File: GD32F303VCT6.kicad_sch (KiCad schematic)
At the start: 32 parts, among them SW1 SKRPACE010, U6 GD32F303VCT6, Y1 TAXM8M4RDBCCT2T, Y2 XKXGI-SUA-32.768K

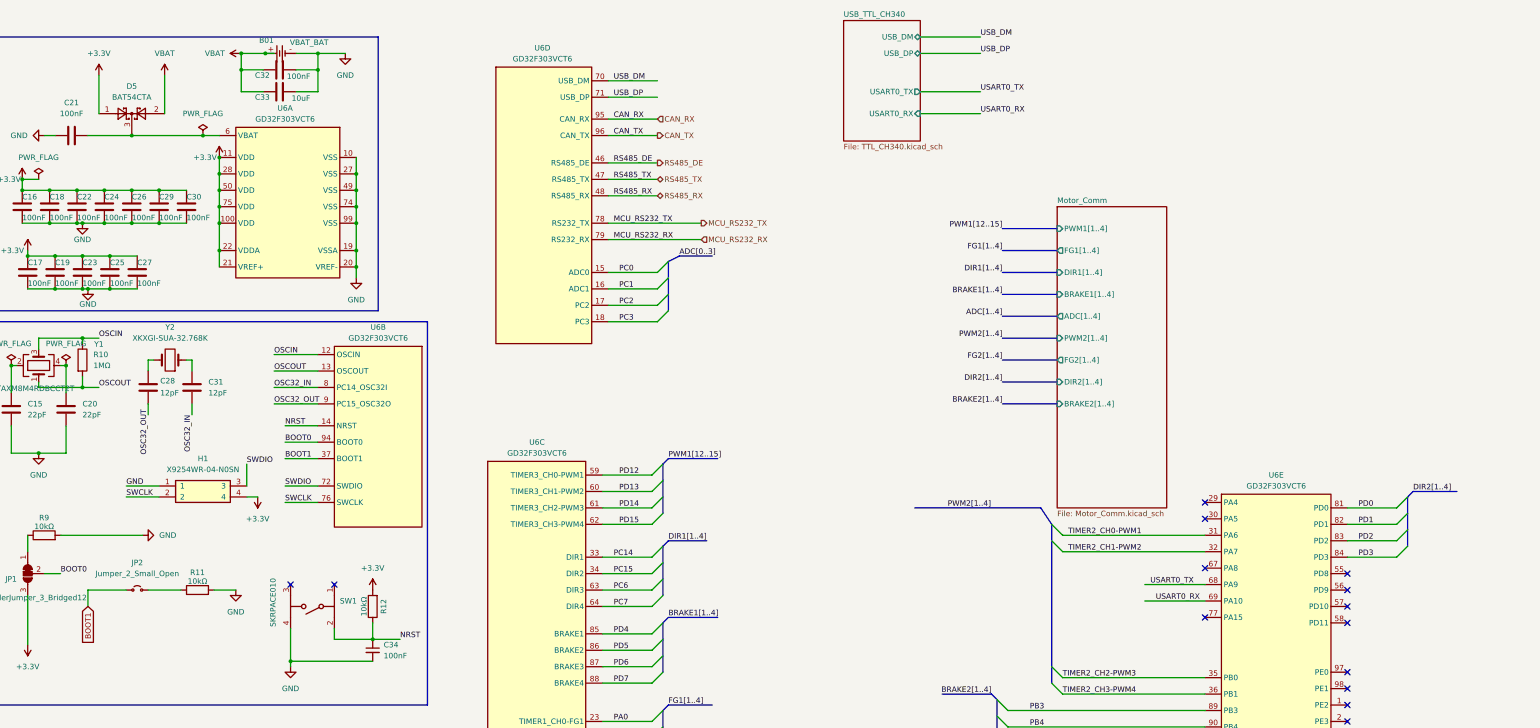
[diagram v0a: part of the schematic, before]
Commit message: 完成GD32F303控制板原理图与PCB设计
- 更新电源、CAN、RS232、RS485及电机通信子电路
- 切换并完善GD32F303VCT6核心原理图
- 新增PCB布局及所需符号、封装库文件
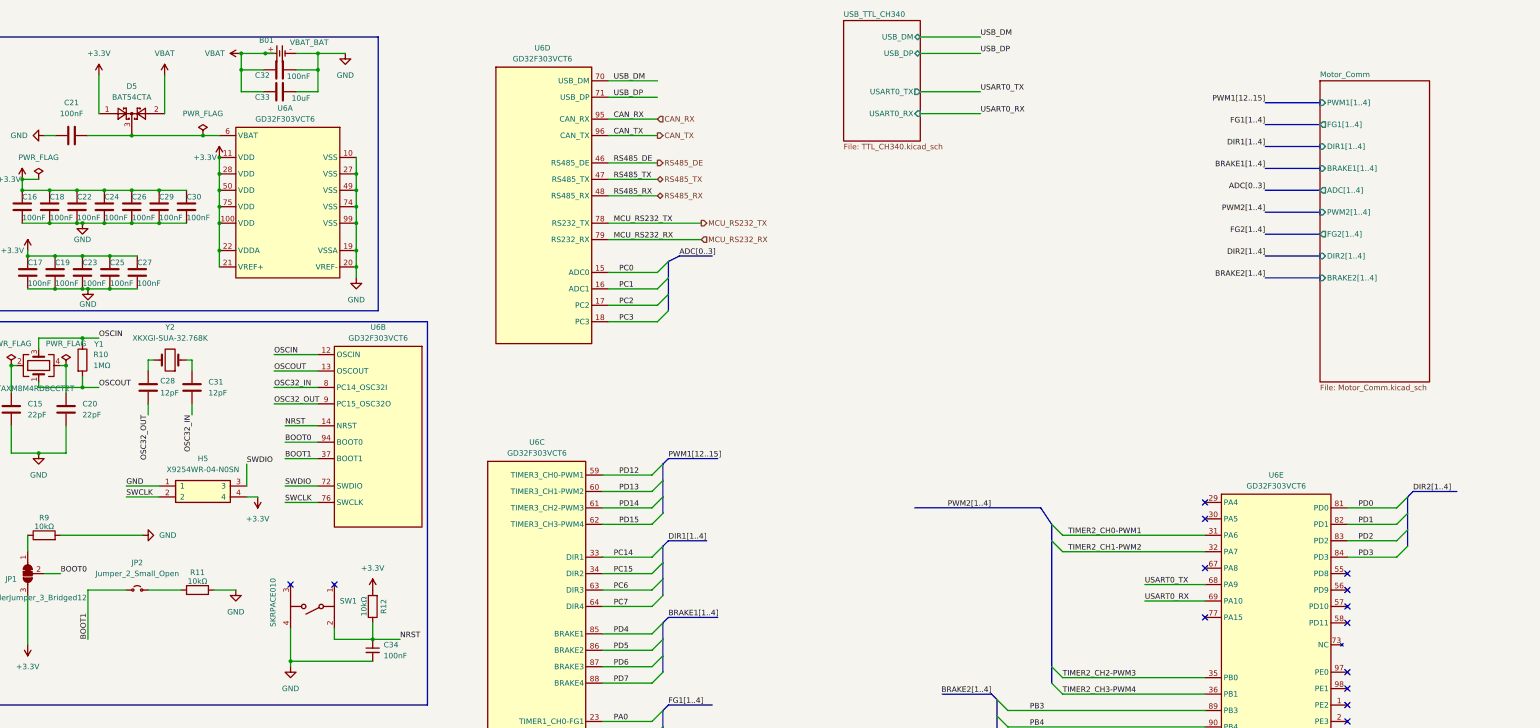
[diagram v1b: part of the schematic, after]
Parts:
- C15: footprint (none) -> Capacitor_SMD:C_0603_1608Metric_Pad1.08x0.95mm_HandSolder
- C16, C17, C18, C19, C20, C21, C22, C23, C24, C25, C26, C27, C28, C29, C30, C31, C32, C33, C34: footprint (none) -> Capacitor_SMD:C_0603_1608Metric
- JP1: footprint (none) -> Jumper:SolderJumper-3_P1.3mm_Bridged12_RoundedPad1.0x1.5mm
- JP2: footprint (none) -> Connector_PinHeader_2.54mm:PinHeader_1x02_P2.54mm_Vertical
- R10, R11, R12, R9: footprint (none) -> Resistor_SMD:R_0603_1608Metric_Pad0.98x0.95mm_HandSolder
- renumbered H1 to H5

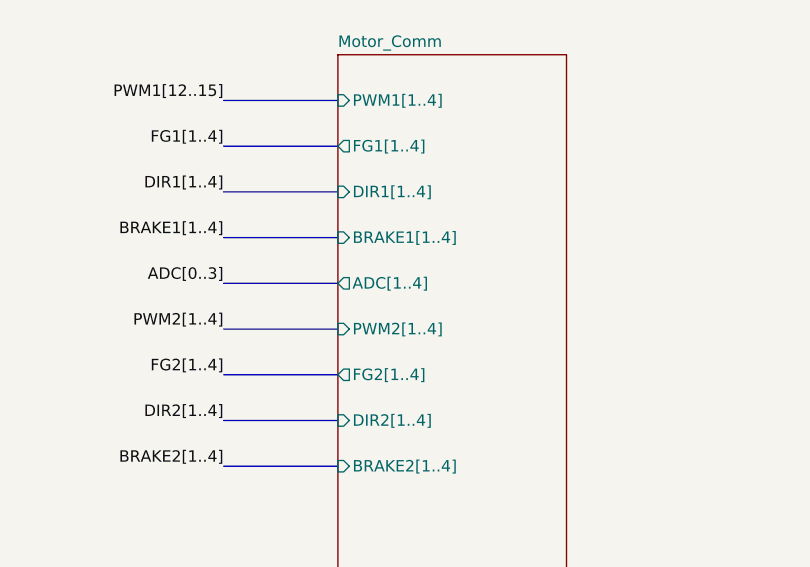
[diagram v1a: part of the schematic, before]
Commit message: 优化接口原理图与PCB布局
- 精简CAN接口并调整各子页器件编号
- 更新电源输入端子与Type-C接口封装
- 重新整理控制板PCB器件布局
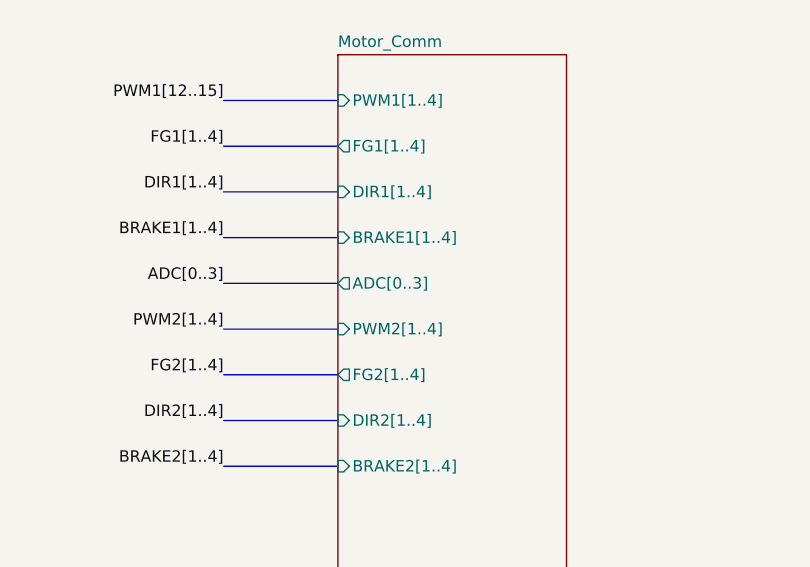
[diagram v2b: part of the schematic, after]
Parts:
- H5: footprint kicad_api_lib:X9254WR-04-N0SN -> Connector_PinHeader_2.54mm:PinHeader_1x04_P2.54mm_Vertical
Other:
- sheet Motor_Comm ports: added ADC[0..3]; removed ADC[1..4]
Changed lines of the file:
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@@
 			)
 		)
-		(property "Footprint" "kicad_api_lib:X9254WR-04-N0SN"
+		(property "Footprint" "Connector_PinHeader_2.54mm:PinHeader_1x04_P2.54mm_Vertical"
 			(at 67.31 125.73 0)
 			(hide yes)
@@
 			)
 		)
-		(pin "ADC[1..4]" output
+		(pin "ADC[0..3]" output
 			(at 326.39 60.96 180)
 			(effects

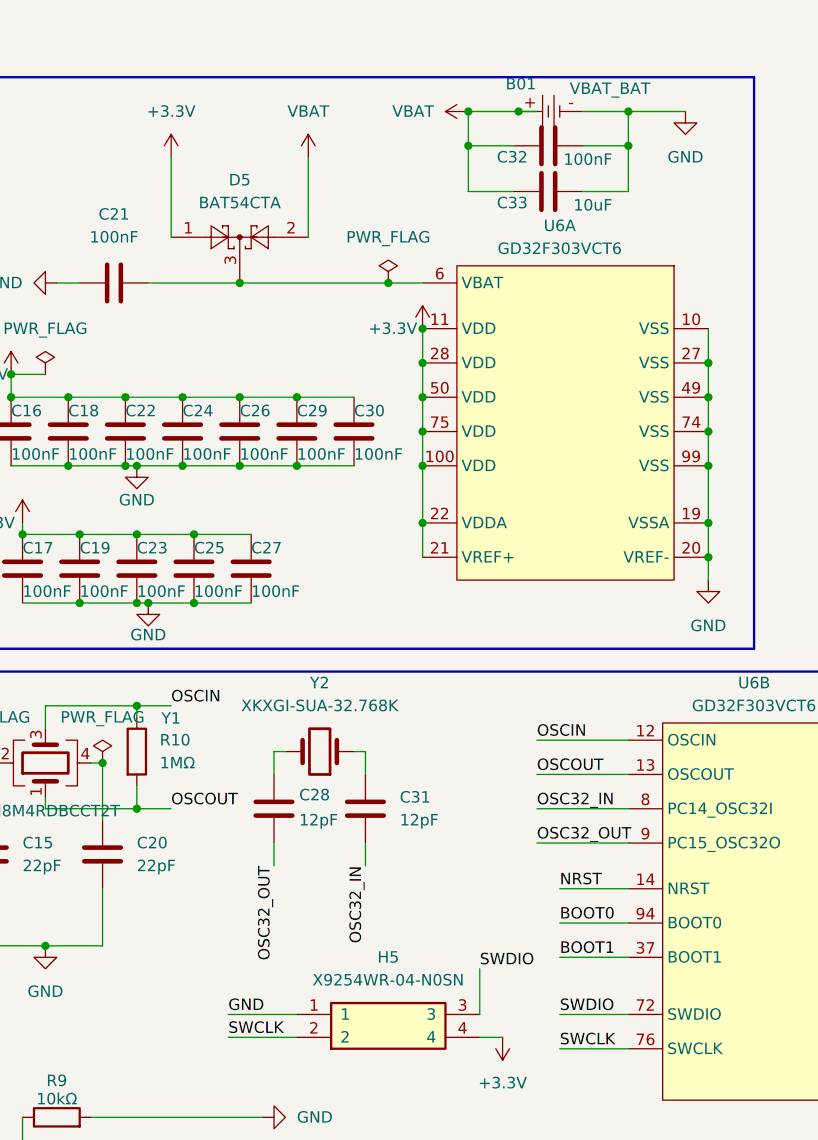
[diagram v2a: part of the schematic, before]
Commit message: 完善PCB布线与接口电源网络
- 调整控制板PCB器件布局与走线
- 更新MCU、电源及通信接口原理图
- 统一隔离接口地和电源网络标签并修正封装属性
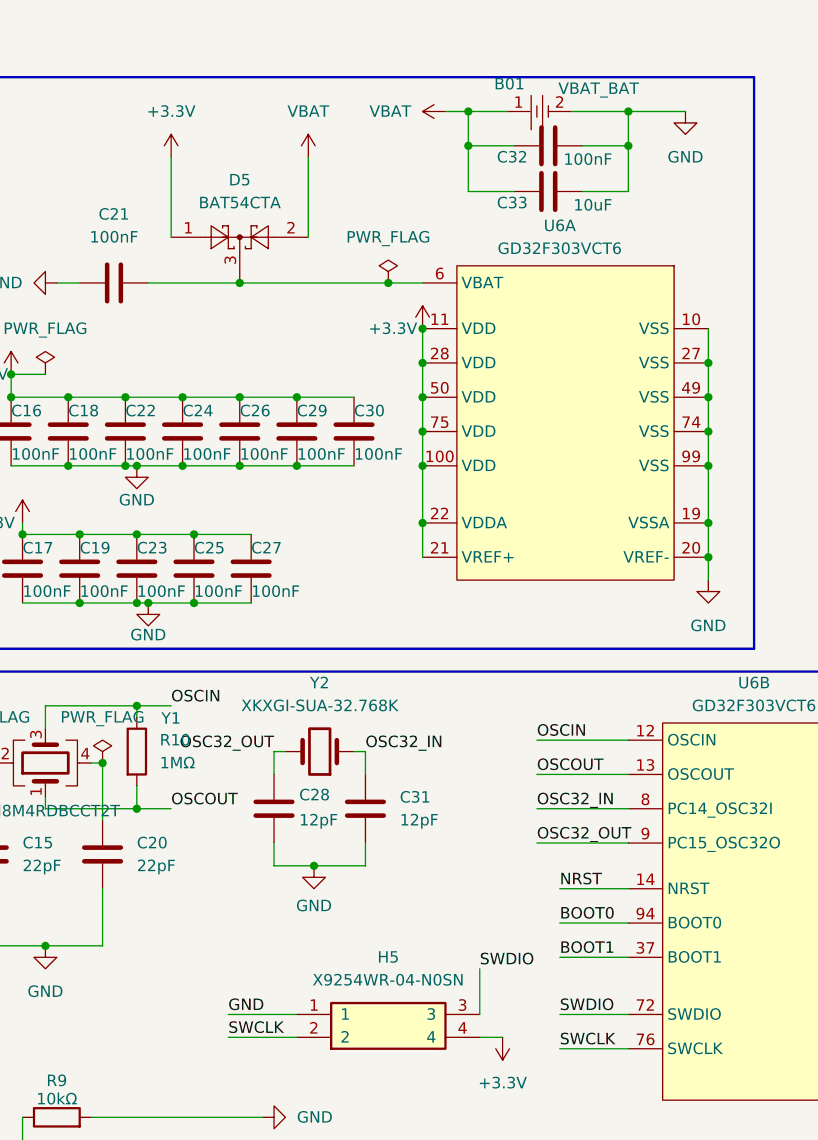
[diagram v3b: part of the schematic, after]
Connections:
- net GND: now also C28.1, C31.1
- net OSC32_IN: now also C31.2, Y2.1; no longer C31.1
- net OSC32_OUT: now also C28.2, Y2.2; no longer C28.1
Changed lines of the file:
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@@
 	)
 	(junction
+		(at 76.2 29.21)
+		(diameter 0)
+		(color 0 0 0 0)
+	)
+	(junction
 		(at 71.12 60.96)
 		(diameter 0)
@@
 	)
 	(junction
-		(at 81.788 29.21)
-		(diameter 0)
-		(color 0 0 0 0)
-	)
-	(junction
 		(at 45.72 83.82)
 		(diameter 0)
@@
 	)
 	(junction
-		(at 76.2 29.21)
-		(diameter 0)
-		(color 0 0 0 0)
-	)
-	(junction
 		(at 50.8 60.96)
 		(diameter 0)
@@
 	)
 	(junction
+		(at 59.055 113.03)
+		(diameter 0)
+		(color 0 0 0 0)
+	)
+	(junction
 		(at 67.31 48.26)
 		(diameter 0)
@@
 	(wire
 		(pts
+			(xy 59.055 113.03) (xy 64.77 113.03)
+		)
+		(stroke
+			(width 0)
+			(type default)
+		)
+	)
+	(wire
+		(pts
 			(xy 34.29 140.97) (xy 53.34 140.97)
 		)
@@
 	(wire
 		(pts
-			(xy 81.788 29.21) (xy 83.82 29.21)
+			(xy 160.02 134.62) (xy 171.45 134.62)
 		)
 		(stroke
@@
 	(wire
 		(pts
-			(xy 160.02 134.62) (xy 171.45 134.62)
+			(xy 81.28 38.1) (xy 76.2 38.1)
 		)
 		(stroke
@@
 	(wire
 		(pts
-			(xy 81.28 38.1) (xy 76.2 38.1)
+			(xy 93.98 29.21) (xy 100.33 29.21)
 		)
 		(stroke
@@
 	(wire
 		(pts
-			(xy 93.98 29.21) (xy 100.33 29.21)
+			(xy 54.61 113.03) (xy 59.055 113.03)
+		)
+		(stroke
+			(width 0)
+			(type default)
+		)
+	)
+	(wire
+		(pts
+			(xy 73.66 29.21) (xy 76.2 29.21)
 		)
 		(stroke
@@
 	(wire
 		(pts
-			(xy 88.9 29.21) (xy 93.98 29.21)
-		)
-		(stroke
-			(width 0)
-			(type default)
-		)
-	)
-	(wire
-		(pts
 			(xy 43.18 106.68) (xy 39.37 106.68)
 		)
@@
 		)
 	)
-	(wire
+	(bus
 		(pts
-			(xy 76.2 29.21) (xy 81.788 29.21)
+			(xy 173.99 181.61) (xy 175.26 180.34)
 		)
 		(stroke
@@
 		)
 	)
-	(bus
+	(wire
 		(pts
-			(xy 173.99 181.61) (xy 175.26 180.34)
+			(xy 29.21 106.68) (xy 29.21 105.41)
 		)
 		(stroke
@@
 	(wire
 		(pts
-			(xy 29.21 106.68) (xy 29.21 105.41)
+			(xy 106.68 165.1) (xy 106.68 161.29)
 		)
 		(stroke
@@
 	(wire
 		(pts
-			(xy 106.68 165.1) (xy 106.68 161.29)
+			(xy 38.1 60.96) (xy 44.45 60.96)
 		)
 		(stroke
@@
 	(wire
 		(pts
-			(xy 38.1 60.96) (xy 44.45 60.96)
+			(xy 22.86 107.95) (xy 22.86 101.6)
 		)
 		(stroke
@@
 	(wire
 		(pts
-			(xy 22.86 107.95) (xy 22.86 101.6)
+			(xy 87.63 29.21) (xy 93.98 29.21)
 		)
 		(stroke
@@
 	(wire
 		(pts
+			(xy 80.518 29.21) (xy 76.2 29.21)
+		)
+		(stroke
+			(width 0)
+			(type default)
+		)
+	)
+	(wire
+		(pts
 			(xy 93.98 29.21) (xy 93.98 33.02)
 		)
@@
 		)
 	)
-	(label "OSC32_IN"
-		(at 64.77 113.03 270)
-		(effects
-			(font
-				(size 1.27 1.27)
-			)
-			(justify right bottom)
-		)
-	)
 	(label "BRAKE1[1..4]"
 		(at 175.26 160.02 0)
@@
 		)
 	)
-	(label "OSC32_OUT"
-		(at 54.61 113.03 270)
-		(effects
-			(font
-				(size 1.27 1.27)
-			)
-			(justify right bottom)
-		)
-	)
 	(label "SWDIO"
 		(at 86.36 129.54 0)
@@
 		)
 	)
+	(label "OSC32_IN"
+		(at 64.77 100.33 0)
+		(effects
+			(font
+				(size 1.27 1.27)
+			)
+			(justify left bottom)
+		)
+	)
+	(label "OSC32_OUT"
+		(at 54.61 100.33 180)
+		(effects
+			(font
+				(size 1.27 1.27)
+			)
+			(justify right bottom)
+		)
+	)
 	(label "PC7"
 		(at 162.56 157.48 0)
@@
 	)
 	(symbol
+		(lib_id "power:GND")
+		(at 59.055 113.03 0)
+		(unit 1)
+		(body_style 1)
+		(exclude_from_sim no)
+		(in_bom yes)
+		(on_board yes)
+		(in_pos_files yes)
+		(dnp no)
+		(fields_autoplaced yes)
+		(property "Reference" "#PWR089"
+			(at 59.055 119.38 0)
+			(hide yes)
+			(show_name no)
+			(do_not_autoplace no)
+			(effects
+				(font
+					(size 1.27 1.27)
+				)
+			)
+		)
+		(property "Value" "GND"
+			(at 59.055 117.475 0)
+			(show_name no)
+			(do_not_autoplace no)
+			(effects
+				(font
+					(size 1.27 1.27)
+				)
+			)
+		)
+		(property "Footprint" ""
+			(at 59.055 113.03 0)
+			(hide yes)
+			(show_name no)
+			(do_not_autoplace no)
+			(effects
+				(font
+					(size 1.27 1.27)
+				)
+			)
+		)
+		(property "Datasheet" ""
+			(at 59.055 113.03 0)
+			(hide yes)
+			(show_name no)
+			(do_not_autoplace no)
+			(effects
+				(font
+					(size 1.27 1.27)
+				)
+			)
+		)
+		(property "Description" "Power symbol creates a global label with name \"GND\" , ground"
+			(at 59.055 113.03 0)
+			(hide yes)
+			(show_name no)
+			(do_not_autoplace no)
+			(effects
+				(font
+					(size 1.27 1.27)
+				)
+			)
+		)
+		(pin "1"
+		)
+		(instances
+			(project "GD32F303"
+				(path "/54005433-e3aa-4693-8f75-bb73943288d3/ab5b236f-20a8-4993-b87c-2c1c522e6f92"
+					(reference "#PWR089")
+					(unit 1)
+				)
+			)
+		)
+	)
+	(symbol
 		(lib_id "Device:C")
 		(at 31.75 64.77 0)
@@
 	(symbol
 		(lib_id "PZ254V-11-02P:VBAT_BAT")
-		(at 87.63 24.892 0)
+		(at 86.36 24.892 0)
 		(unit 1)
 		(body_style 1)
 		(exclude_from_sim no)
-		(in_bom no)
-		(on_board no)
+		(in_bom yes)
+		(on_board yes)
 		(in_pos_files yes)
 		(dnp no)
 		(property "Reference" "B01"
-			(at 82.042 26.162 0)
+			(at 80.772 26.162 0)
 			(show_name no)
 			(do_not_autoplace no)
@@
 		)
 		(property "Value" "VBAT_BAT"
-			(at 91.948 26.67 0)
+			(at 90.678 26.67 0)
 			(show_name no)
 			(do_not_autoplace no)
@@
 			)
 		)
-		(property "Footprint" "Battery:BatteryHolder_Keystone_500"
-			(at 87.63 24.892 0)
+		(property "Footprint" "Resistor_SMD:R_0603_1608Metric"
+			(at 86.36 24.892 0)
 			(hide yes)
 			(show_name no)
@@
 		)
 		(property "Datasheet" ""
-			(at 87.63 24.892 0)
+			(at 86.36 24.892 0)
 			(hide yes)
 			(show_name no)
@@
 		)
 		(property "Description" ""
-			(at 87.63 24.892 0)
+			(at 86.36 24.892 0)
 			(hide yes)
 			(show_name no)
@@
 			)
 		)
-		(pin "+"
+		(pin "1"
 		)
-		(pin "-"
+		(pin "2"
 		)
 		(instances
@@
 	(symbol
 		(lib_id "power:+BATT")
-		(at 76.2 29.21 90)
+		(at 73.66 29.21 90)
 		(unit 1)
 		(body_style 1)
@@
 		(fields_autoplaced yes)
 		(property "Reference" "#PWR040"
-			(at 80.01 29.21 0)
+			(at 77.47 29.21 0)
 			(hide yes)
 			(show_name no)
@@
 		)
 		(property "Value" "VBAT"
-			(at 72.39 29.2099 90)
+			(at 69.85 29.2099 90)
 			(show_name no)
 			(do_not_autoplace no)
@@
 		)
 		(property "Footprint" ""
-			(at 76.2 29.21 0)
+			(at 73.66 29.21 0)
 			(hide yes)
 			(show_name no)
@@
 		)
 		(property "Datasheet" ""
-			(at 76.2 29.21 0)
+			(at 73.66 29.21 0)
 			(hide yes)
 			(show_name no)
@@
 		)
 		(property "Description" "Power symbol creates a global label with name \"+BATT\""
-			(at 76.2 29.21 0)
+			(at 73.66 29.21 0)
 			(hide yes)
 			(show_name no)

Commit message: 标记MCU核心页预留电容为DNP
将C32和C33设置为不装配，更新生产装配属性。
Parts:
- C32, C33: now not fitted
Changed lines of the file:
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@@
 		(on_board yes)
 		(in_pos_files yes)
-		(dnp no)
+		(dnp yes)
 		(property "Reference" "C33"
 			(at 82.804 39.37 90)
@@
 		(on_board yes)
 		(in_pos_files yes)
-		(dnp no)
+		(dnp yes)
 		(property "Reference" "C32"
 			(at 82.804 34.29 90)

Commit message: 保存商业化布局优化前工程版本
- 保存当前PCB布局与走线调整
- 更新MCU核心页器件属性
- 记录后续商业板布局优化前的可回退检查点
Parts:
- C32, C33: now left out of the parts list
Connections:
- net GND: no longer C32.2, C33.2, D5.2
- new net VBAT: C32.2, C33.2, D5.2
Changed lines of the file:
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@@
 	)
 	(junction
-		(at 76.2 29.21)
-		(diameter 0)
-		(color 0 0 0 0)
-	)
-	(junction
 		(at 71.12 60.96)
 		(diameter 0)
@@
 	)
 	(junction
-		(at 93.98 29.21)
-		(diameter 0)
-		(color 0 0 0 0)
-	)
-	(junction
 		(at 87.63 170.18)
 		(diameter 0)
@@
 	)
 	(junction
+		(at 93.98 29.21)
+		(diameter 0)
+		(color 0 0 0 0)
+	)
+	(junction
 		(at 59.055 113.03)
 		(diameter 0)
@@
 		(color 0 0 0 0)
 	)
+	(junction
+		(at 76.2 29.21)
+		(diameter 0)
+		(color 0 0 0 0)
+	)
 	(no_connect
 		(at 299.72 204.47)
@@
 		)
 	)
+	(wire
+		(pts
+			(xy 90.932 29.21) (xy 93.98 29.21)
+		)
+		(stroke
+			(width 0)
+			(type default)
+		)
+	)
 	(bus
 		(pts
@@
 	(wire
 		(pts
-			(xy 29.21 106.68) (xy 29.21 105.41)
+			(xy 76.2 29.21) (xy 77.47 29.21)
 		)
 		(stroke
@@
 	(wire
 		(pts
-			(xy 106.68 165.1) (xy 106.68 161.29)
+			(xy 29.21 106.68) (xy 29.21 105.41)
 		)
 		(stroke
@@
 	(wire
 		(pts
-			(xy 38.1 60.96) (xy 44.45 60.96)
+			(xy 106.68 165.1) (xy 106.68 161.29)
 		)
 		(stroke
@@
 	(wire
 		(pts
-			(xy 22.86 107.95) (xy 22.86 101.6)
+			(xy 38.1 60.96) (xy 44.45 60.96)
 		)
 		(stroke
@@
 	(wire
 		(pts
-			(xy 87.63 29.21) (xy 93.98 29.21)
+			(xy 22.86 107.95) (xy 22.86 101.6)
 		)
 		(stroke
@@
 	(wire
 		(pts
-			(xy 80.518 29.21) (xy 76.2 29.21)
-		)
-		(stroke
-			(width 0)
-			(type default)
-		)
-	)
-	(wire
-		(pts
 			(xy 93.98 29.21) (xy 93.98 33.02)
 		)
@@
 		(body_style 1)
 		(exclude_from_sim no)
-		(in_bom yes)
-		(on_board yes)
+		(in_bom no)
+		(on_board no)
 		(in_pos_files yes)
 		(dnp yes)
@@
 	(symbol
 		(lib_id "PZ254V-11-02P:VBAT_BAT")
-		(at 86.36 24.892 0)
+		(at 89.662 25.4 0)
 		(unit 1)
 		(body_style 1)
 		(exclude_from_sim no)
-		(in_bom yes)
+		(in_bom no)
 		(on_board yes)
 		(in_pos_files yes)
 		(dnp no)
 		(property "Reference" "B01"
-			(at 80.772 26.162 0)
+			(at 84.074 26.67 0)
 			(show_name no)
 			(do_not_autoplace no)
@@
 		)
 		(property "Value" "VBAT_BAT"
-			(at 90.678 26.67 0)
+			(at 84.074 31.75 0)
 			(show_name no)
 			(do_not_autoplace no)
@@
 			)
 		)
-		(property "Footprint" "Resistor_SMD:R_0603_1608Metric"
-			(at 86.36 24.892 0)
+		(property "Footprint" "Battery:BatteryHolder_Keystone_500"
+			(at 89.662 25.4 0)
 			(hide yes)
 			(show_name no)
@@
 		)
 		(property "Datasheet" ""
-			(at 86.36 24.892 0)
+			(at 89.662 25.4 0)
 			(hide yes)
 			(show_name no)
@@
 		)
 		(property "Description" ""
-			(at 86.36 24.892 0)
+			(at 89.662 25.4 0)
 			(hide yes)
 			(show_name no)
@@
 		(body_style 1)
 		(exclude_from_sim no)
-		(in_bom yes)
-		(on_board yes)
+		(in_bom no)
+		(on_board no)
 		(in_pos_files yes)
 		(dnp yes)

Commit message: 修复控制总线连接并更新PCB工程文档
规范 PWM、DIR、BRAKE、FG 与 ADC 总线及成员标签，保存最新 PCB 和 KiCad 工程配置，新增工程使用文档。
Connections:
- net PA0 renamed FG1_1
- net PA1 renamed FG1_2
- net PA2 renamed FG1_3
- net PA3 renamed FG1_4
- net PB3 renamed BRAKE2_1
- net PB4 renamed BRAKE2_2
- net PB5 renamed BRAKE2_3
- net PB6 renamed BRAKE2_4
- net PC0 renamed ADC_0
- net PC1 renamed ADC_1
- net PC14 renamed DIR1_1
- net PC15 renamed DIR1_2
- net PC2 renamed ADC_2
- net PC3 renamed ADC_3
- net PC6 renamed DIR1_3
- net PC7 renamed DIR1_4
- net PD0 renamed DIR2_1
- net PD1 renamed DIR2_2
- net PD12 renamed PWM1_1
- net PD13 renamed PWM1_2
- net PD14 renamed PWM1_3
- net PD15 renamed PWM1_4
- net PD2 renamed DIR2_3
- net PD3 renamed DIR2_4
- net PD4 renamed BRAKE1_1
- net PD5 renamed BRAKE1_2
- net PD6 renamed BRAKE1_3
- net PD7 renamed BRAKE1_4
- net TIMER0_CH0-FG1 renamed FG2_1
- net TIMER0_CH1-FG2 renamed FG2_2
- net TIMER0_CH2-FG3 renamed FG2_3
- net TIMER0_CH3-FG4 renamed FG2_4
- net TIMER2_CH0-PWM1 renamed PWM2_1
- net TIMER2_CH1-PWM2 renamed PWM2_2
- net TIMER2_CH2-PWM3 renamed PWM2_3
- net TIMER2_CH3-PWM4 renamed PWM2_4
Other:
- sheet Motor_Comm ports: added ADC_[0..3], BRAKE1_[1..4], BRAKE2_[1..4], DIR1_[1..4], DIR2_[1..4], FG1_[1..4], FG2_[1..4], PWM1_[1..4], PWM2_[1..4]; removed ADC[0..3], BRAKE1[1..4], BRAKE2[1..4], DIR1[1..4], DIR2[1..4], FG1[1..4], FG2[1..4], PWM1[1..4], PWM2[1..4]
